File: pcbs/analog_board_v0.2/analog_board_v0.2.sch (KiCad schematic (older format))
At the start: 3 parts

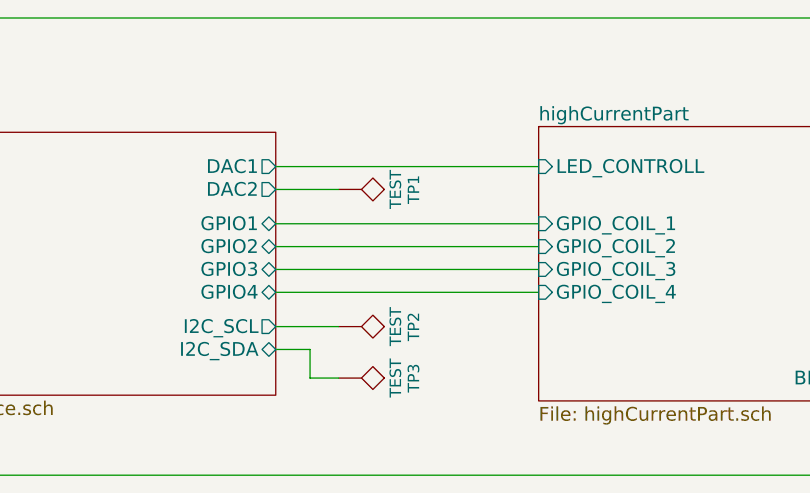
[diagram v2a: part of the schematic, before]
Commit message: Small changes on the backplane standing out.
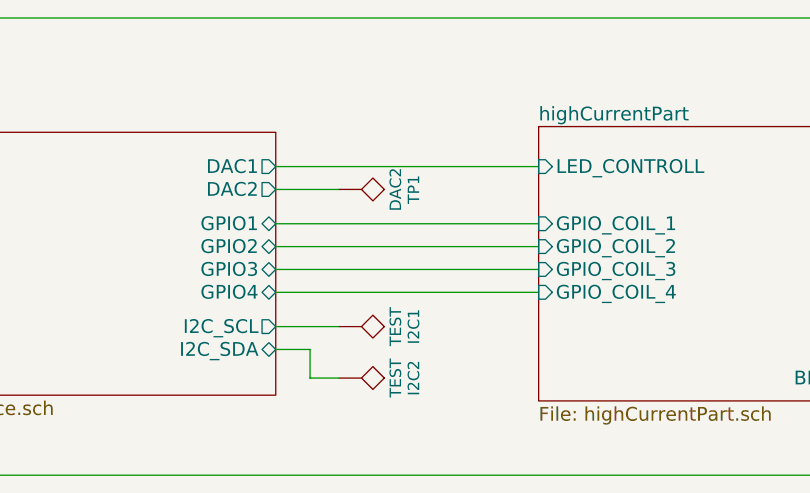
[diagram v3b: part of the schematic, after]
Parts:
- TP1: value TEST -> DAC2
- renumbered TP2 to I2C1, TP3 to I2C2
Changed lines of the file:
@@
 $EndSheet
 $Comp
-L +3.3V #PWR3
+L +3.3V #PWR01
 U 1 1 59551FE0
 P 4475 3125
-F 0 "#PWR3" H 4475 2975 50  0001 C CNN
+F 0 "#PWR01" H 4475 2975 50  0001 C CNN
 F 1 "+3.3V" H 4475 3265 50  0000 C CNN
 F 2 "" H 4475 3125 50  0001 C CNN
@@
 	4825 3125 4475 3125
 $Comp
-L GND #PWR4
+L GND #PWR02
 U 1 1 595520F8
 P 4475 3225
-F 0 "#PWR4" H 4475 2975 50  0001 C CNN
+F 0 "#PWR02" H 4475 2975 50  0001 C CNN
 F 1 "GND" H 4475 3075 50  0000 C CNN
 F 2 "" H 4475 3225 50  0001 C CNN
@@
 	4475 3225 4825 3225
 $Comp
-L +5V #PWR2
+L +5V #PWR03
 U 1 1 59552732
 P 4475 2875
-F 0 "#PWR2" H 4475 2725 50  0001 C CNN
+F 0 "#PWR03" H 4475 2725 50  0001 C CNN
 F 1 "+5V" H 4475 3015 50  0000 C CNN
 F 2 "" H 4475 2875 50  0001 C CNN
@@
 	6525 3575 7675 3575
 $Comp
-L TEST TP2
+L TEST I2C1
 U 1 1 59577F16
 P 6800 3725
-F 0 "TP2" H 6800 4025 50  0000 C BNN
+F 0 "I2C1" H 6800 4025 50  0000 C BNN
 F 1 "TEST" H 6800 3975 50  0000 C CNN
 F 2 "Tespoints:TP_SMD_quadr_1mm" H 6800 3725 50  0001 C CNN
@@
 $EndComp
 $Comp
-L TEST TP3
+L TEST I2C2
 U 1 1 59578158
 P 6800 3950
-F 0 "TP3" H 6800 4250 50  0000 C BNN
+F 0 "I2C2" H 6800 4250 50  0000 C BNN
 F 1 "TEST" H 6800 4200 50  0000 C CNN
 F 2 "Tespoints:TP_SMD_quadr_1mm" H 6800 3950 50  0001 C CNN
@@
 P 6800 3125
 F 0 "TP1" H 6800 3425 50  0000 C BNN
-F 1 "TEST" H 6800 3375 50  0000 C CNN
+F 1 "DAC2" H 6800 3375 50  0000 C CNN
 F 2 "Tespoints:TP_SMD_quadr_1mm" H 6800 3125 50  0001 C CNN
 F 3 "" H 6800 3125 50  0001 C CNN
@@
 	1375 3175 1850 3175
 $Comp
-L +3.3V #PWR1
+L +3.3V #PWR04
 U 1 1 59593859
 P 1500 3025
-F 0 "#PWR1" H 1500 2875 50  0001 C CNN
+F 0 "#PWR04" H 1500 2875 50  0001 C CNN
 F 1 "+3.3V" H 1500 3165 50  0000 C CNN
 F 2 "" H 1500 3025 50  0001 C CNN
